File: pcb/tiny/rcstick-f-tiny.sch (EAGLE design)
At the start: 41 parts, among them J1 MOLEX_48037-0001, J2 2212S, SW1 SKRPACE010, U1 STM32F042K6U6, U2 CC2500, U3 MCP1703AT-3302E/CB, X1 16MHz/10pF, X2 26MHz/9pF, X3 (50 Ohm)

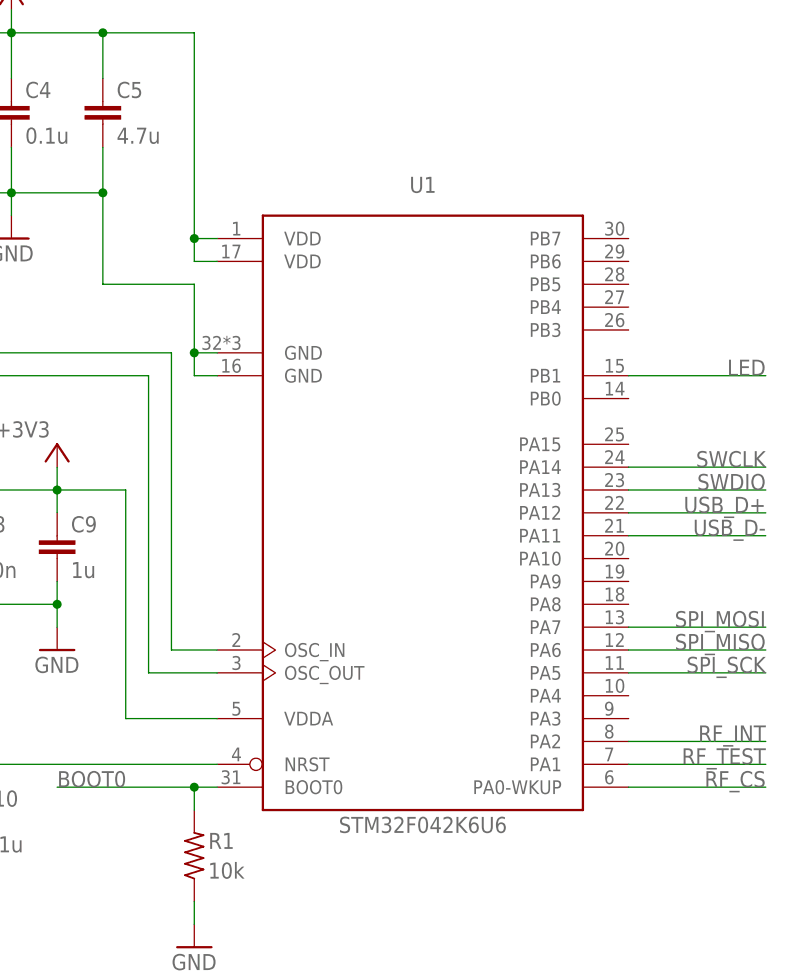
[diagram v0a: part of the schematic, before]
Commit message: fix minor issue of tiny artwork
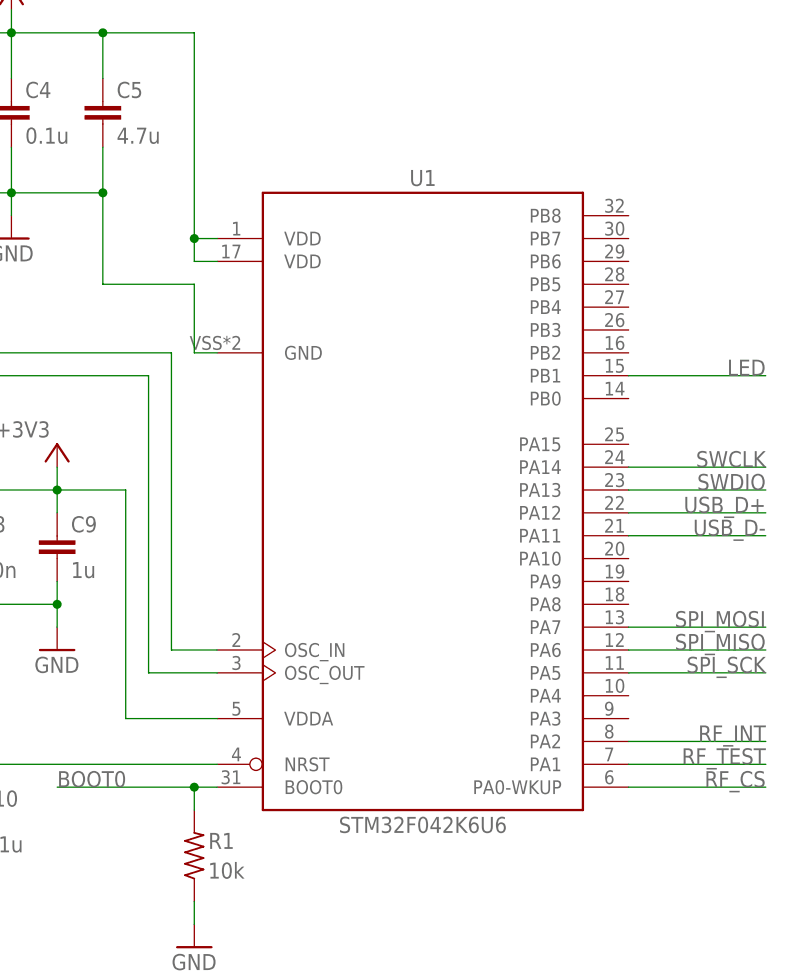
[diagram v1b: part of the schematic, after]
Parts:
- U1: device stm32:STM32F042KTUQFPN32-M -> stm32:STM32F042K6U-M
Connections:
- net GND: now also U1.GND; no longer U1.GND@1, U1.GND@2
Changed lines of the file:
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@@
 <?xml version="1.0" encoding="utf-8"?>
 <!DOCTYPE eagle SYSTEM "eagle.dtd">
-<eagle version="9.6.1">
+<eagle version="9.6.2">
 <drawing>
 <settings>
@@
 <part name="+3V2" library="supply1" library_urn="urn:adsk.eagle:library:371" deviceset="+3V3" device=""/>
 <part name="GND3" library="supply1" library_urn="urn:adsk.eagle:library:371" deviceset="GND" device=""/>
-<part name="U1" library="stm32" library_urn="urn:adsk.eagle:library:7041200" deviceset="STM32F042K*T" device="UQFPN32-M" package3d_urn="urn:adsk.eagle:package:20323426/7" value="STM32F042K6U6"/>
+<part name="U1" library="stm32" library_urn="urn:adsk.eagle:library:7041200" deviceset="STM32F042K6U" device="-M" package3d_urn="urn:adsk.eagle:package:20323426/7" value="STM32F042K6U6"/>
 <part name="C3" library="gen-discrete3" library_urn="urn:adsk.eagle:library:8961849" deviceset="RCL_C-EU" device="C0402-HS" package3d_urn="urn:adsk.eagle:package:8961862/2" value="0.1u"/>
 <part name="C4" library="gen-discrete3" library_urn="urn:adsk.eagle:library:8961849" deviceset="RCL_C-EU" device="C0402-HS" package3d_urn="urn:adsk.eagle:package:8961862/2" value="0.1u"/>
@@
 </instance>
 <instance part="U1" gate="G$1" x="99.06" y="106.68" smashed="yes">
-<attribute name="NAME" x="99.06" y="139.7" size="1.778" layer="95" align="bottom-center"/>
+<attribute name="NAME" x="99.06" y="140.462" size="1.778" layer="95" align="bottom-center"/>
 <attribute name="VALUE" x="99.06" y="68.58" size="1.778" layer="96" align="bottom-center"/>
 </instance>
@@
 <pinref part="GND3" gate="1" pin="GND"/>
 <wire x1="53.34" y1="137.16" x2="53.34" y2="139.7" width="0.1524" layer="91"/>
-<pinref part="U1" gate="G$1" pin="GND@2"/>
-<wire x1="76.2" y1="119.38" x2="73.66" y2="119.38" width="0.1524" layer="91"/>
-<wire x1="73.66" y1="119.38" x2="73.66" y2="121.92" width="0.1524" layer="91"/>
 <wire x1="73.66" y1="121.92" x2="73.66" y2="129.54" width="0.1524" layer="91"/>
 <wire x1="73.66" y1="129.54" x2="63.5" y2="129.54" width="0.1524" layer="91"/>
 <wire x1="63.5" y1="129.54" x2="63.5" y2="139.7" width="0.1524" layer="91"/>
 <junction x="63.5" y="139.7"/>
-<pinref part="U1" gate="G$1" pin="GND@1"/>
-<wire x1="76.2" y1="121.92" x2="73.66" y2="121.92" width="0.1524" layer="91"/>
-<junction x="73.66" y="121.92"/>
+<pinref part="U1" gate="G$1" pin="GND"/>
+<wire x1="73.66" y1="121.92" x2="76.2" y2="121.92" width="0.1524" layer="91"/>
 </segment>
 <segment>

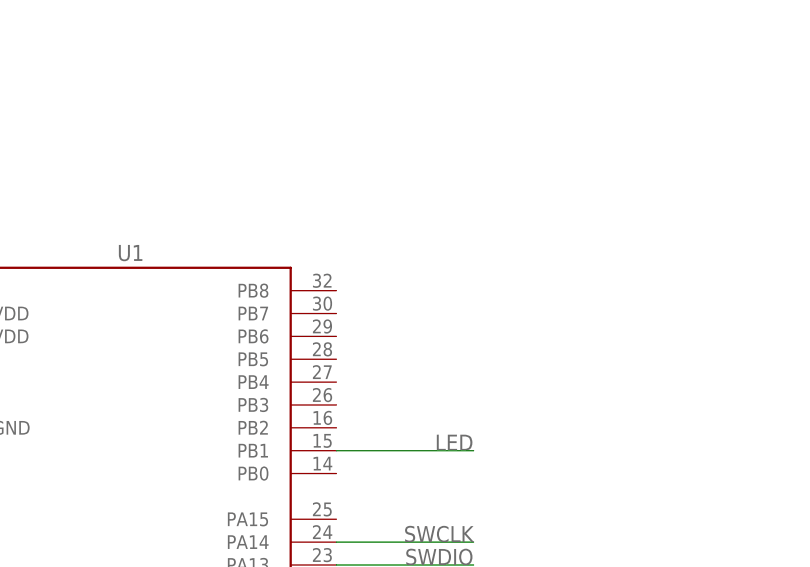
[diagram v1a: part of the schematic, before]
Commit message: added QFN28 MCU version
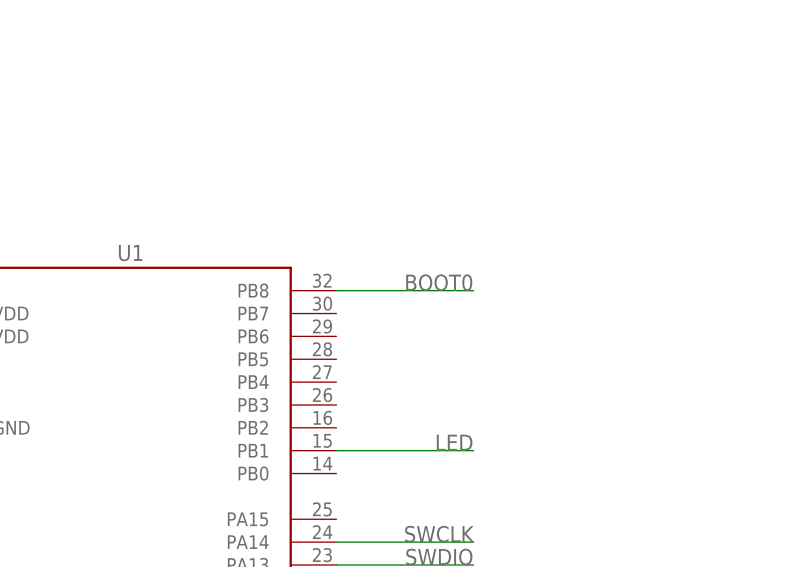
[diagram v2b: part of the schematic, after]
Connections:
- net BOOT0: now also U1.PB8
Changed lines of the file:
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@@
 <label x="218.44" y="17.78" size="1.778" layer="95" rot="MR0"/>
+</segment>
+<segment>
+<pinref part="U1" gate="G$1" pin="PB8"/>
+<wire x1="121.92" y1="137.16" x2="137.16" y2="137.16" width="0.1524" layer="91"/>
+<label x="137.16" y="137.16" size="1.778" layer="95" rot="MR0"/>
 </segment>
 </net>
